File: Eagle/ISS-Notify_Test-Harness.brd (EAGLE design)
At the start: 63.5 x 63.5 mm, 36 parts, among them U1 ATMEGA32U4, U3 TPS63001, X1 8 MHz

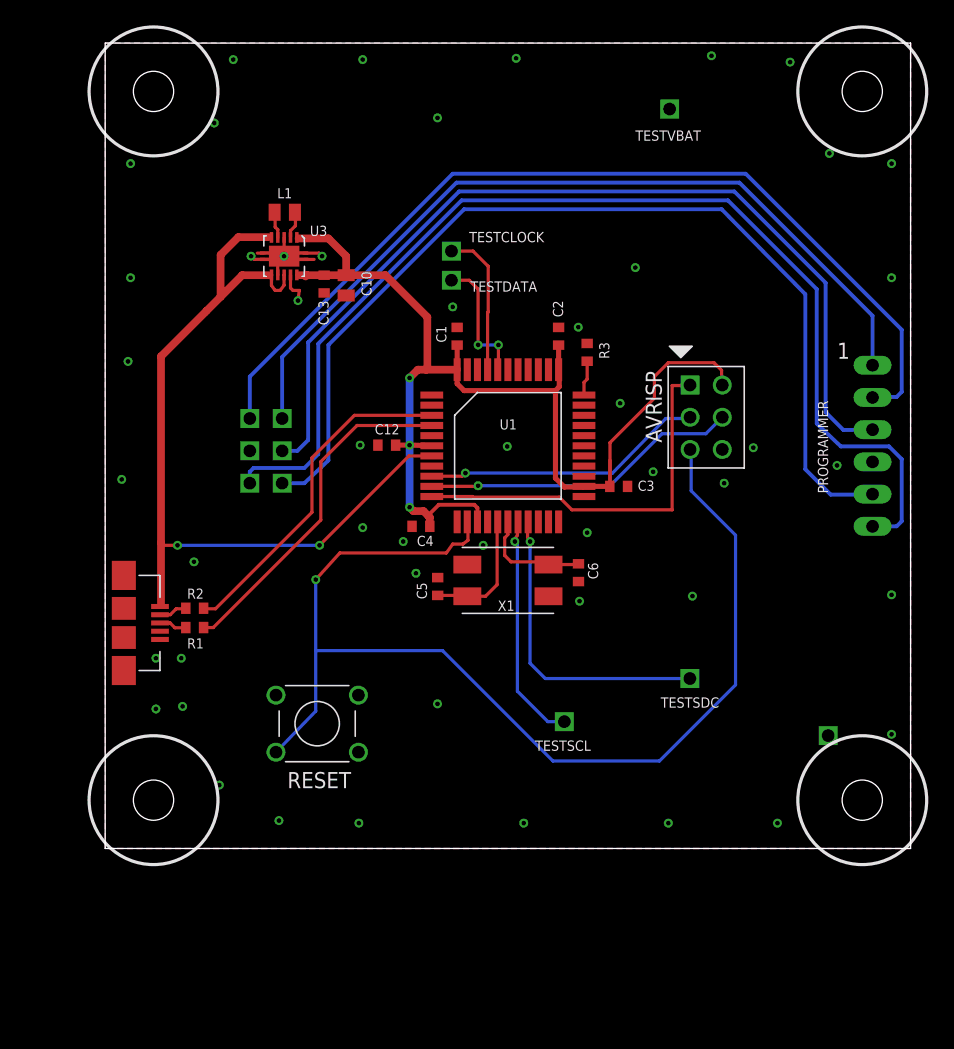
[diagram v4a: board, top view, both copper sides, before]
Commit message: 2 rgb status LEDs
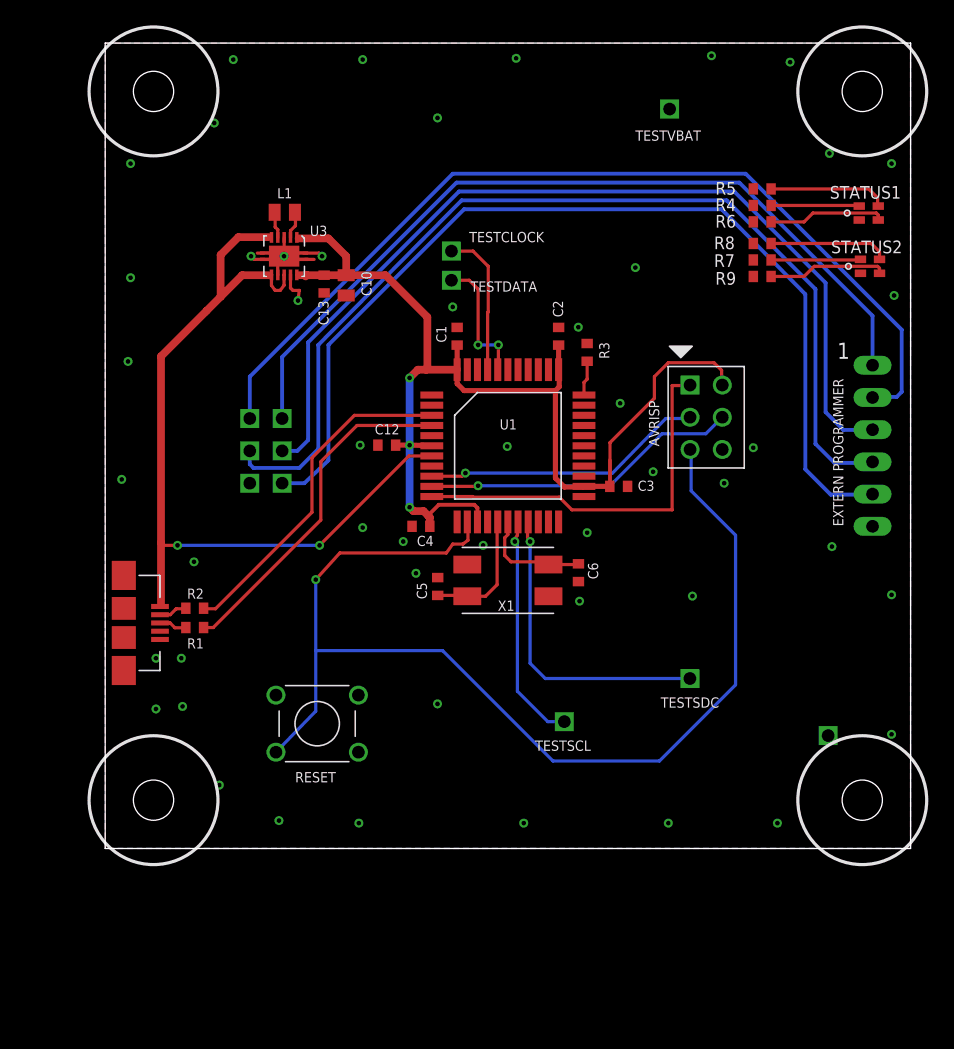
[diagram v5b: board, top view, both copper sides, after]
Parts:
- added R4, R5, R7, R8: 82, rcl_custom:0603-C-NOSILK
- added R6, R9: 10, rcl_custom:0603-C-NOSILK
- added STATUS1, STATUS2: RGBLED, ISS-Notify:SMDRGBLED
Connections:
- removed net TESTGND: JPROGRAMER.6, TESTIGND.1
- new net LED1_B: R6.1, U1.27
- new net LED1_G: R5.1, U1.28
- new net LED1_R: R4.1, U1.29
- new net LED2_B: R9.1, U1.31
- new net LED2_G: R8.1, U1.32
- new net LED2_R: R7.1, U1.26
- new net N$11: R8.2, STATUS2.GREEN
- new net N$12: R9.2, STATUS2.BLUE
- new net N$3: R4.2, STATUS1.RED
- new net N$7: R5.2, STATUS1.GREEN
- new net N$8: R6.2, STATUS1.BLUE
- new net N$9: R7.2, STATUS2.RED
- net GND: now also JPROGRAMER.6, TESTIGND.1
- net TESTMOSI: now also JPROGRAMER.4
- net VCC: now also STATUS1.ANODE, STATUS2.ANODE
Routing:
- net TESTGND: track 88.3 -> 0.00 mm
- net TESTMOSI: track 0.00 -> 79.6 mm
- net N$11: track 0.00 -> 9.42 mm
- net N$7: track 0.00 -> 9.36 mm
- net N$12: track 0.00 -> 9.34 mm
- net N$8: track 0.00 -> 9.20 mm
- net N$9: track 0.00 -> 7.07 mm
- net N$3: track 0.00 -> 6.97 mm
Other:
- board text added: "EXTERN PROGRAMMER"
- board text removed: "PROGRAMMER"

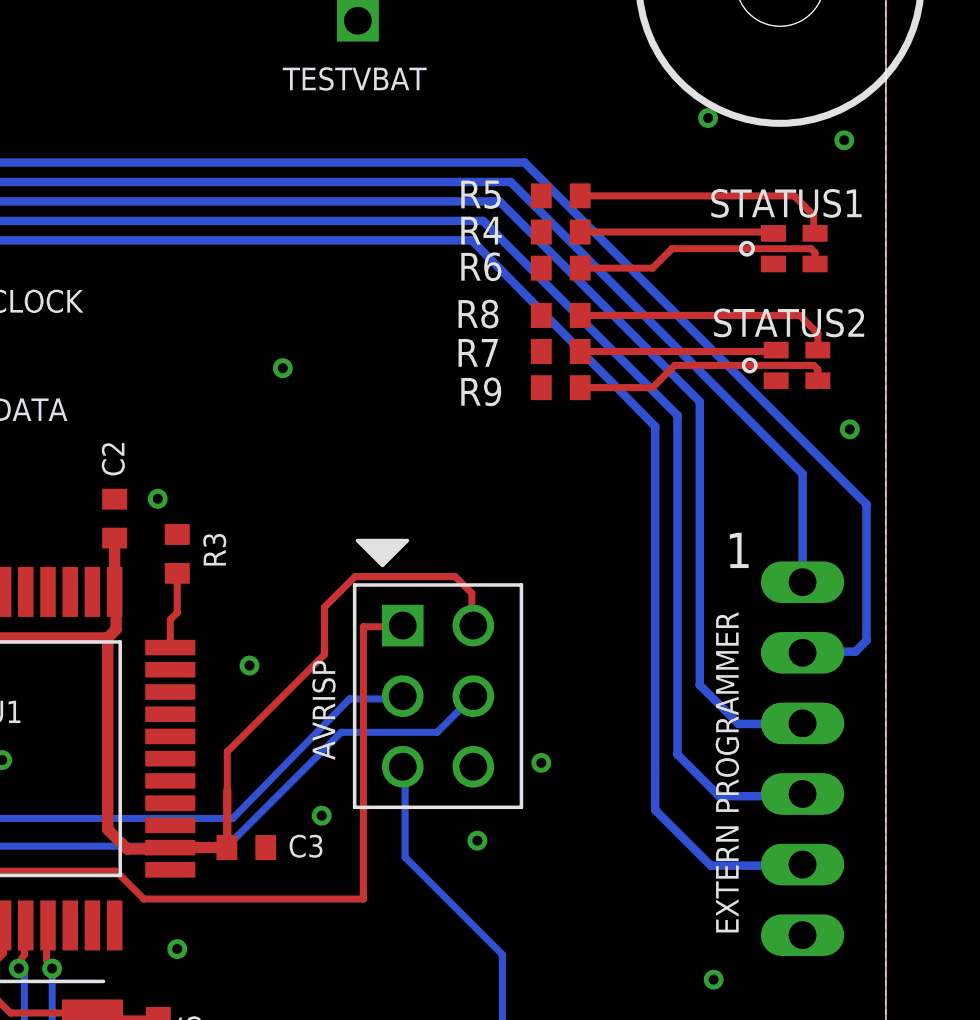
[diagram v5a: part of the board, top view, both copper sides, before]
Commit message: route status LEDs
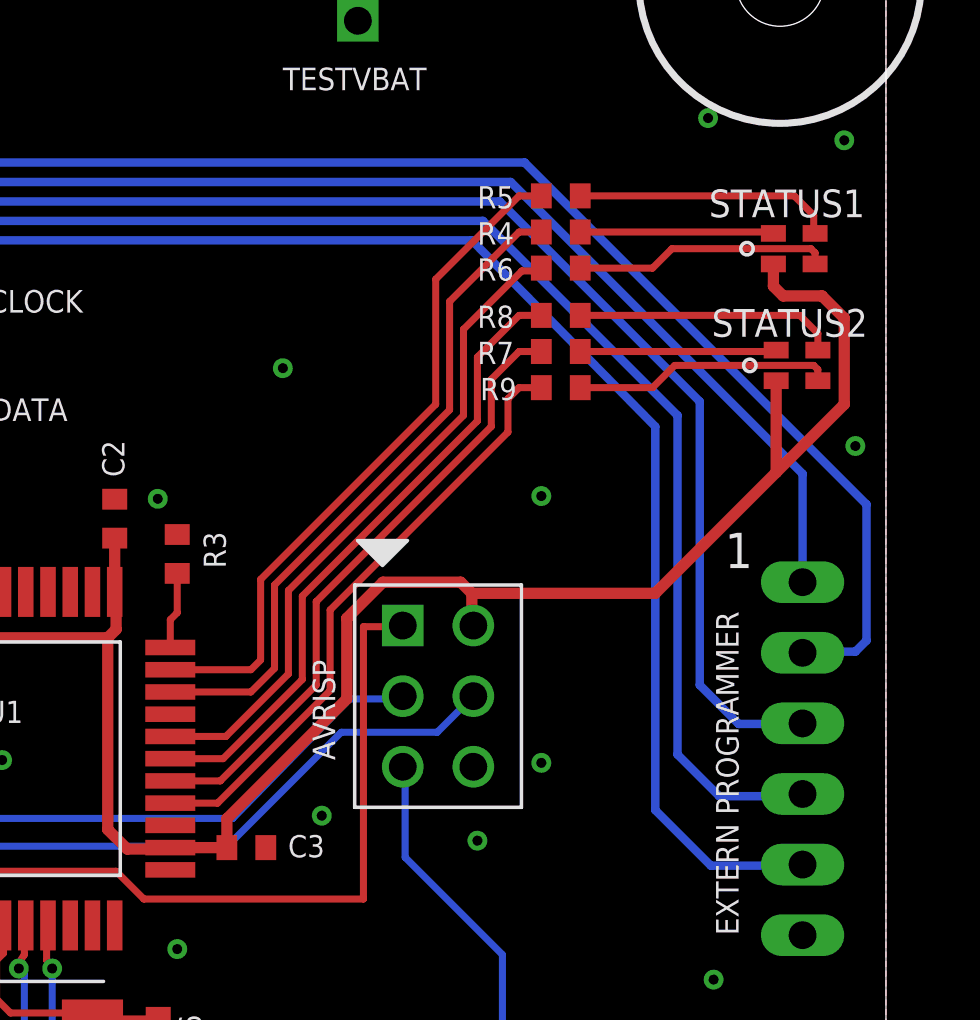
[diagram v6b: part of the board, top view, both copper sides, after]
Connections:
- net LED1_B: now also U1.29; no longer U1.27
- net LED1_G: now also U1.32; no longer U1.28
- net LED1_R: now also U1.31; no longer U1.29
- net LED2_B: now also U1.26; no longer U1.31
- net LED2_G: now also U1.28; no longer U1.32
- net LED2_R: now also U1.27; no longer U1.26
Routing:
- net VCC: track 90.7 -> 116.3 mm
- net LED1_G: track 0.00 -> 24.7 mm
- net LED1_R: track 0.00 -> 24.2 mm
- net LED1_B: track 0.00 -> 23.9 mm
- net LED2_G: track 0.00 -> 23.1 mm
- net LED2_R: track 0.00 -> 22.5 mm
- net LED2_B: track 0.00 -> 21.9 mm

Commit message: move power supply over a little
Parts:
- moved C13 5.02 mm to (13.7, 41.0)
- moved C10 5.02 mm to (15.4, 40.9)
- moved L1 5.02 mm to (10.6, 46.7)
- moved U3 5.02 mm to (10.5, 43.2)
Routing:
- net VIN: track 66.8 -> 61.8 mm
- net VCC: track 116.3 -> 114.8 mm
- net GND: vias 49 -> 51

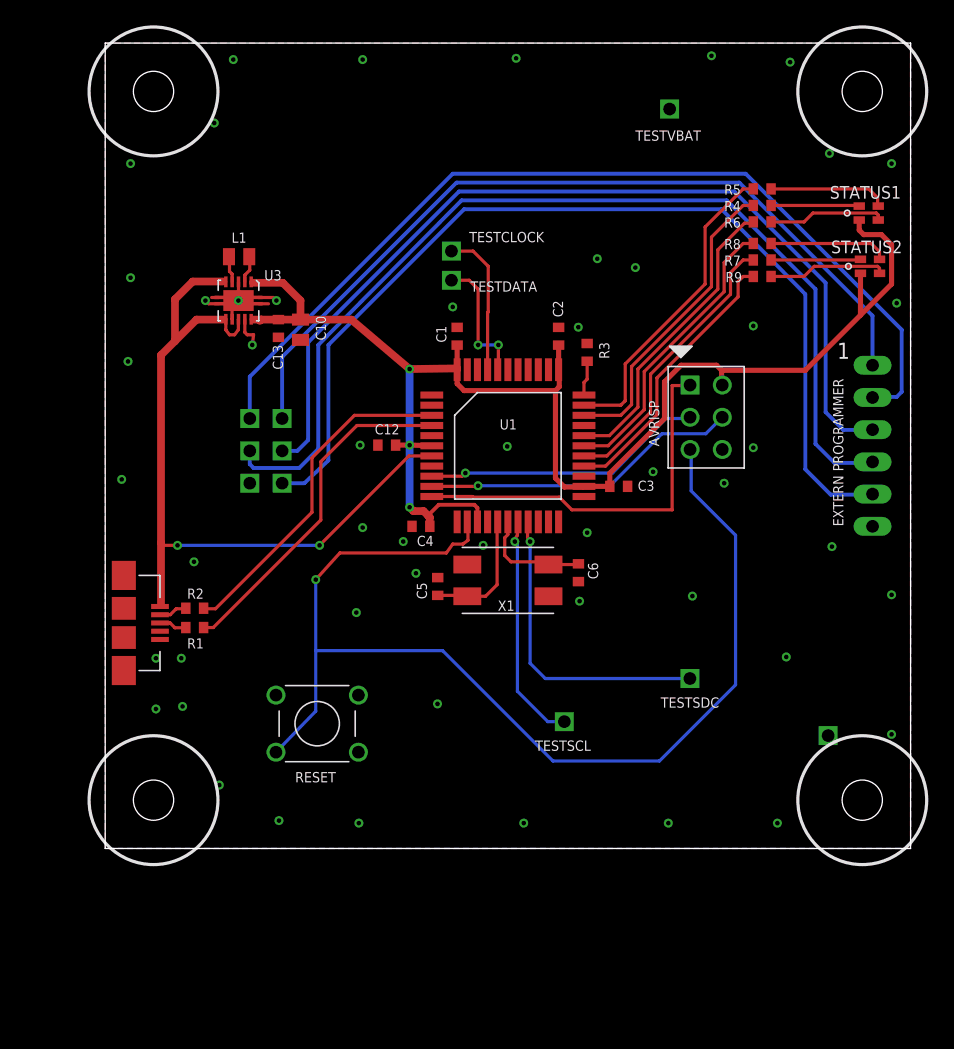
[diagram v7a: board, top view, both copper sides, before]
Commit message: Added LTC1153 package to library. Added to schematic without circuit. Needs another look in the morning.
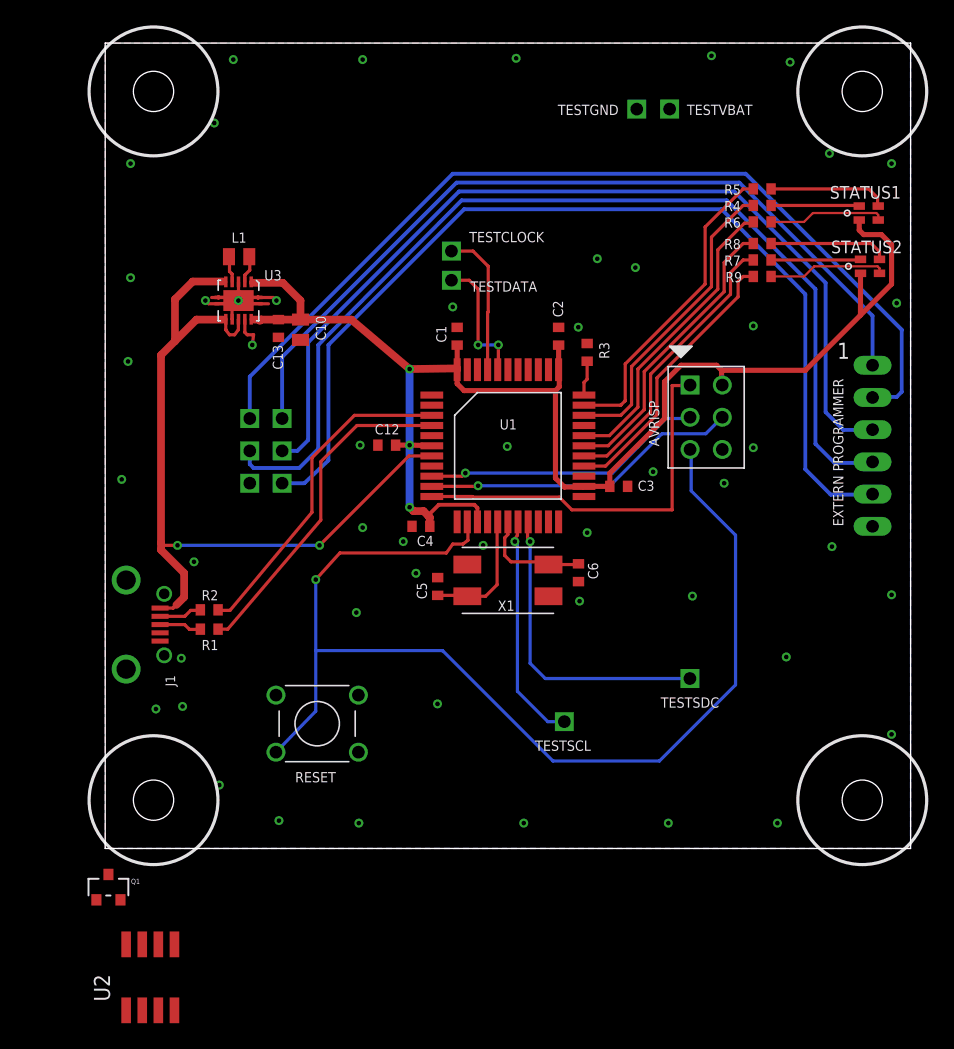
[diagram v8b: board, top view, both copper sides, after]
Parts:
- removed USB: CON_USB-MICRO-6GND, ISS-Notify:USBMICROSMT
- added J1: CON_USB-MICRO-ZX62D-B-5P8, ISS-Notify:USBMICROSMT-HIROSE
- added Q1: NTR4501N-D, max-viz:SOT-23
- added U2: LTC1153CS8, ISS-Notify:SO-8
- moved TESTGND 51.6 mm to (41.9, 58.3)
- moved R1 1.15 mm to (8.20, 17.3)
- moved R2 1.15 mm to (8.20, 18.8)
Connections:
- new net N$13: U1.1
- net GND: now also J1.P$1, J1.P$2, J1.P$3, J1.P$4, J1.P5; no longer USB.5
- net N$4: now also J1.P3; no longer USB.D+
- net N$5: now also J1.P2; no longer USB.D-
- net TESTVCC: now also TESTVBAT.1
- net VCC: now also Q1.3
- net VIN: now also J1.P1; no longer USB.VUSB
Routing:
- net VIN: track 61.8 -> 63.9 mm
- net N$5: track 2.25 -> 3.39 mm
- net N$4: track 2.20 -> 3.34 mm
- net D+: track 27.3 -> 26.6 mm
- net D-: track 26.9 -> 26.2 mm
- net GND: track 9.86 -> 9.94 mm, vias 51 -> 50
